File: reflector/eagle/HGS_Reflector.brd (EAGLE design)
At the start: 100 x 100 mm, 27 parts, among them J1 U.FL, U3 LP2985XX-N

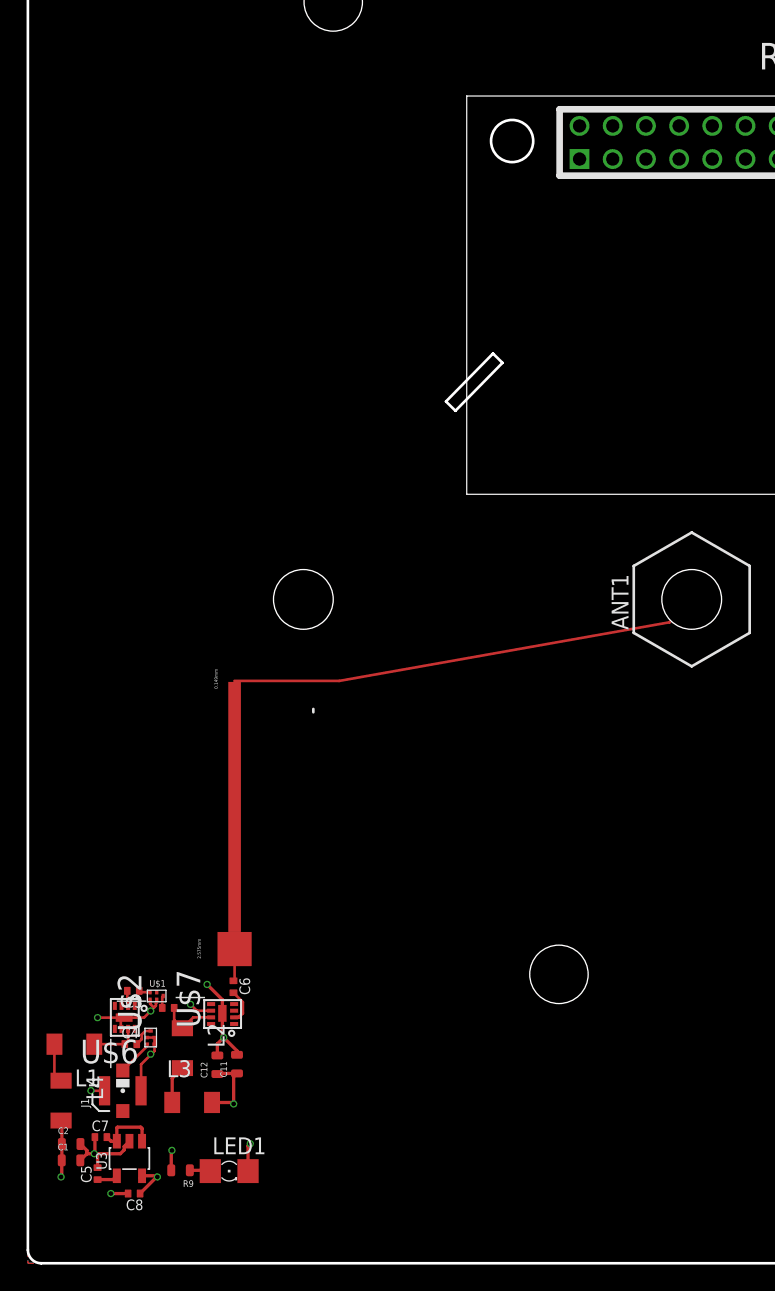
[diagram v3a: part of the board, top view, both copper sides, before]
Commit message: On the HGS board, I positioned the 3.3V regulator so that it is now close to the pin header on the Rasp Pi Zero W, and made a few changes to positions of the other parts to accomodate that.
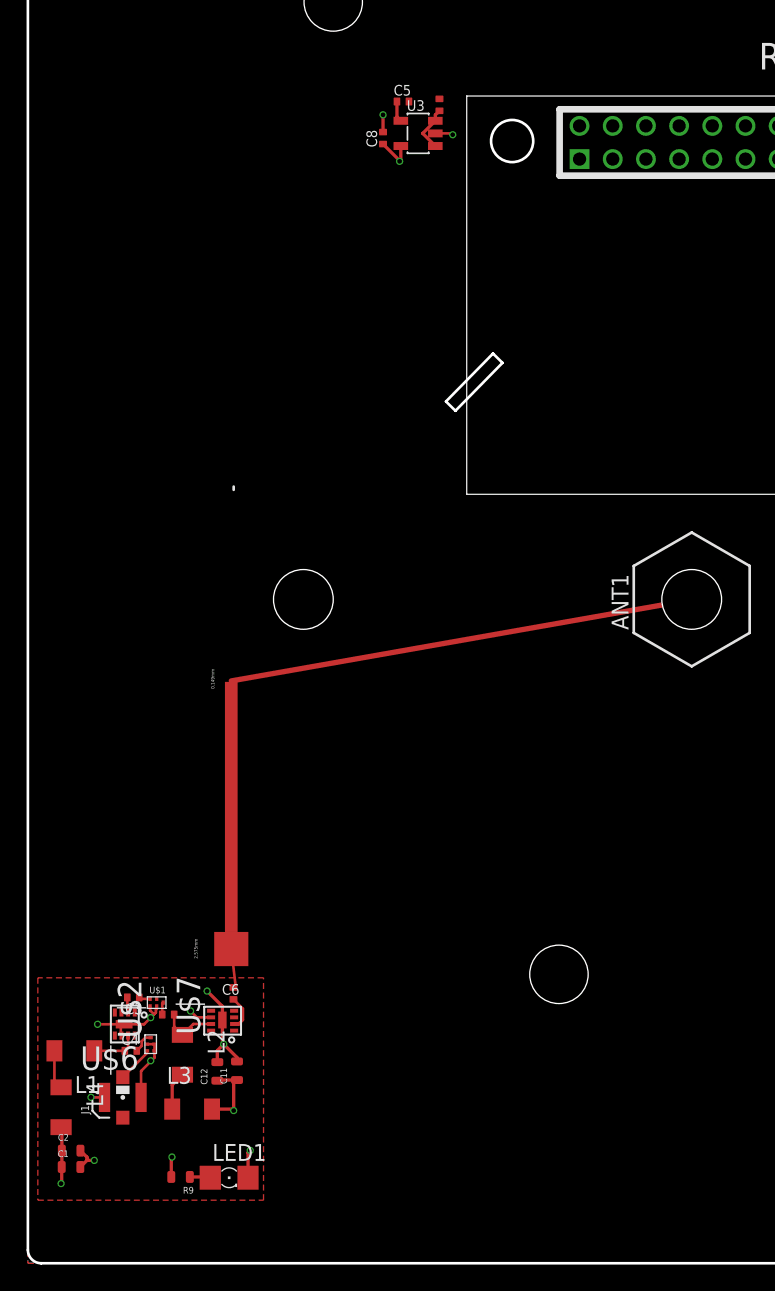
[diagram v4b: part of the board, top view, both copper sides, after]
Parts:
- moved C5 84.0 mm to (28.2, 87.5), turned to 0 degrees
- moved C7 81.8 mm to (31.0, 87.2), turned to 270 degrees
- moved C8 81.7 mm to (26.8, 84.8), turned to 90 degrees
- moved U3 80.2 mm to (29.4, 85.1), turned to 180 degrees
- moved C1 0.50 mm to (3.25, 7.25)
- moved C11 0.50 mm to (15.8, 14.5)
- moved C12 0.50 mm to (14.3, 14.4)
- moved C14 0.50 mm to (10.6, 18.7)
- moved C2 0.50 mm to (3.26, 8.48)
- moved C3 0.50 mm to (7.94, 20.0)
- moved C4 0.50 mm to (7.75, 16.0)
- moved C6 0.50 mm to (15.5, 20.3)
- moved J1 0.50 mm to (7.15, 12.5)
- moved L1 0.50 mm to (3.50, 16.0)
- moved L2 0.50 mm to (11.6, 15.7)
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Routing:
- net GND: track 33.5 -> 29.4 mm, vias 10 -> 11
- net 5V: track 4.81 -> 3.57 mm
- net N$9: track 2.42 -> 3.12 mm

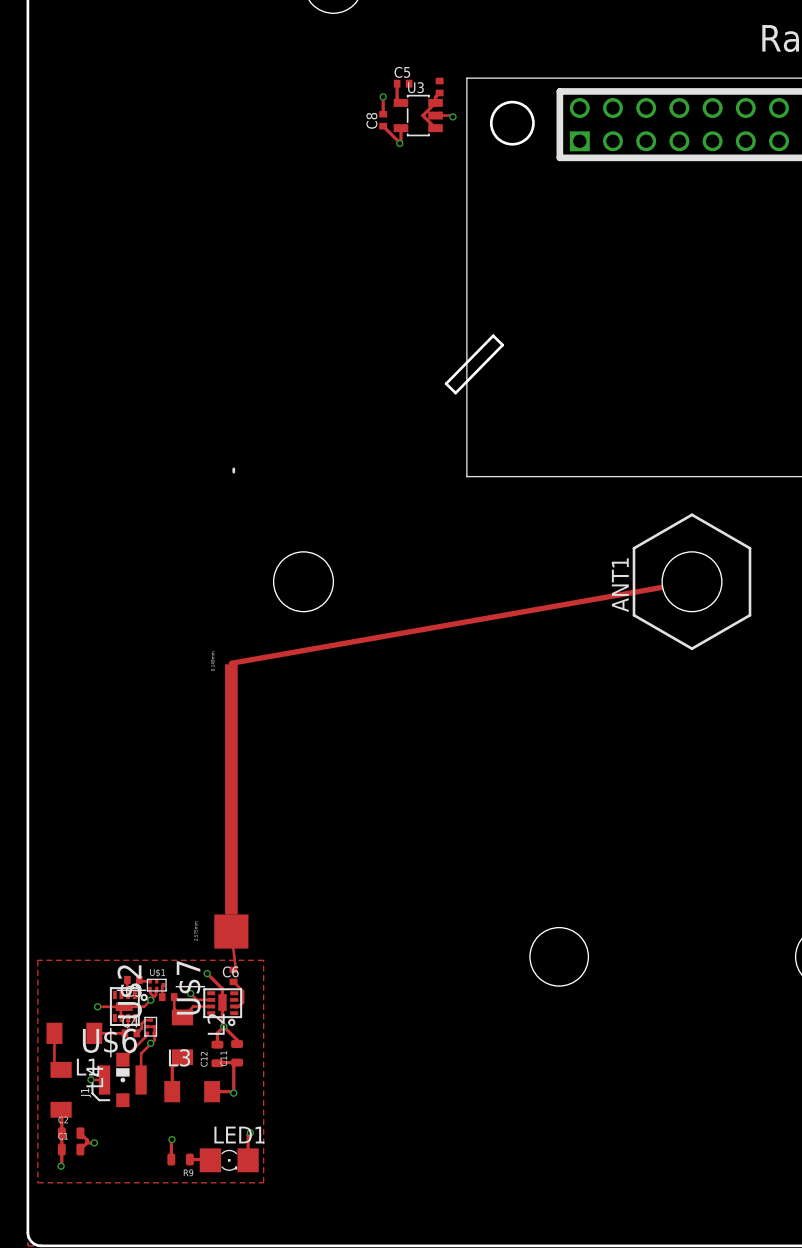
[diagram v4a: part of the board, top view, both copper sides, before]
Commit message: I made sure that all the signals were completely routed, and fixed the clearance issue with the wire going to the center by replacing the center drill hole with a large via that goes directly to the antenna footprint on the top of the board (layer 16).
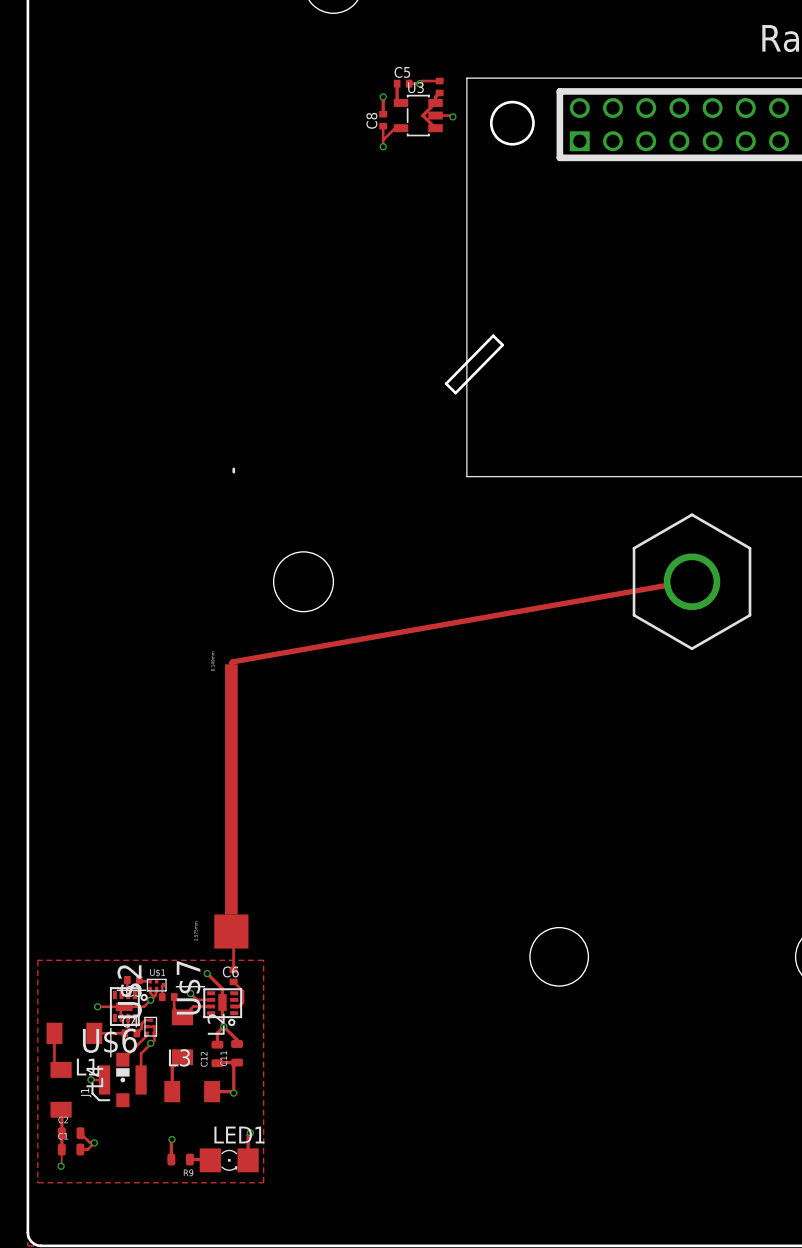
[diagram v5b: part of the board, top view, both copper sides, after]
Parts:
- flipped ANT1 to the bottom
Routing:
- net GND: track 29.4 -> 32.1 mm, vias 11 -> 12
- net N$2: vias 0 -> 1
- added copper zone on layer 15, net 3.3V
- removed copper zone on layer 15, net GND

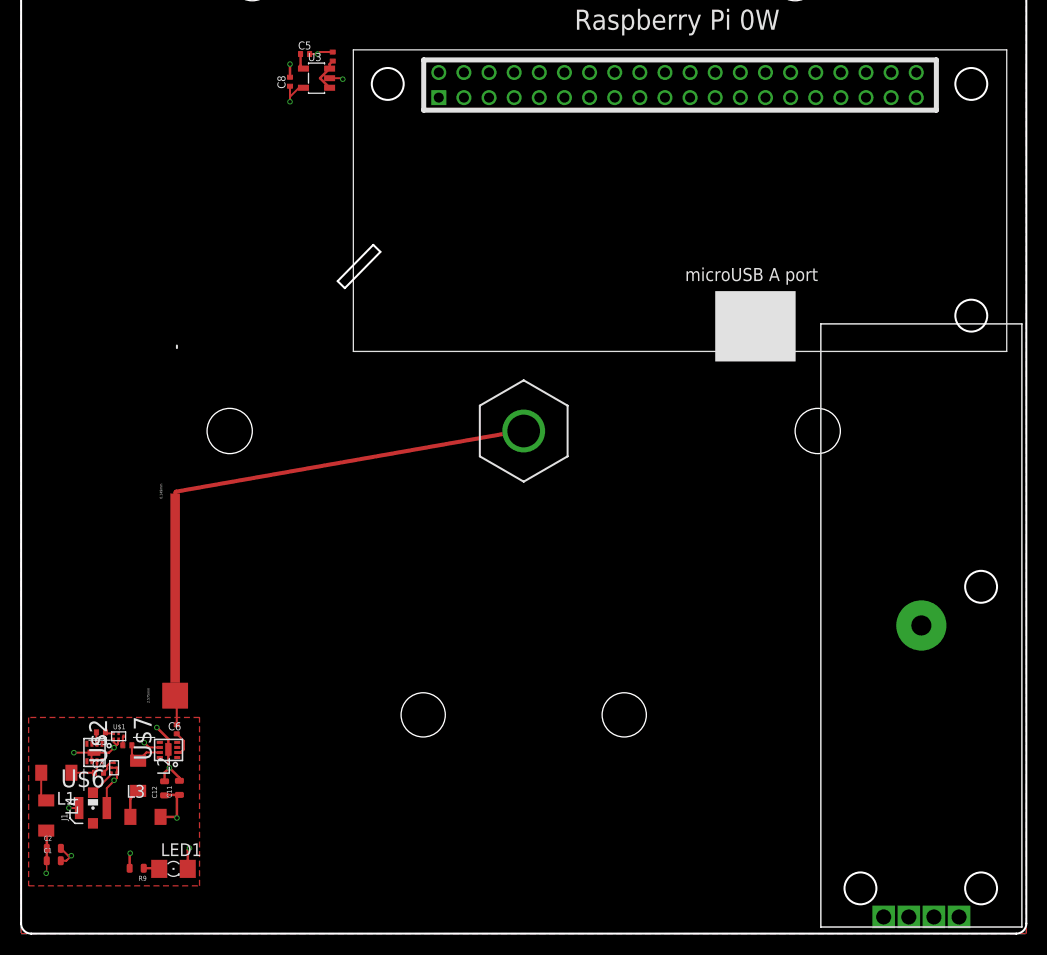
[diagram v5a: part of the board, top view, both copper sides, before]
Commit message: I finalized the schematic and routing of the board for HGS. Note that I adjusted the dxf layer by adding a fourth drill hole underneath the atheros card. It is ready for a design review.
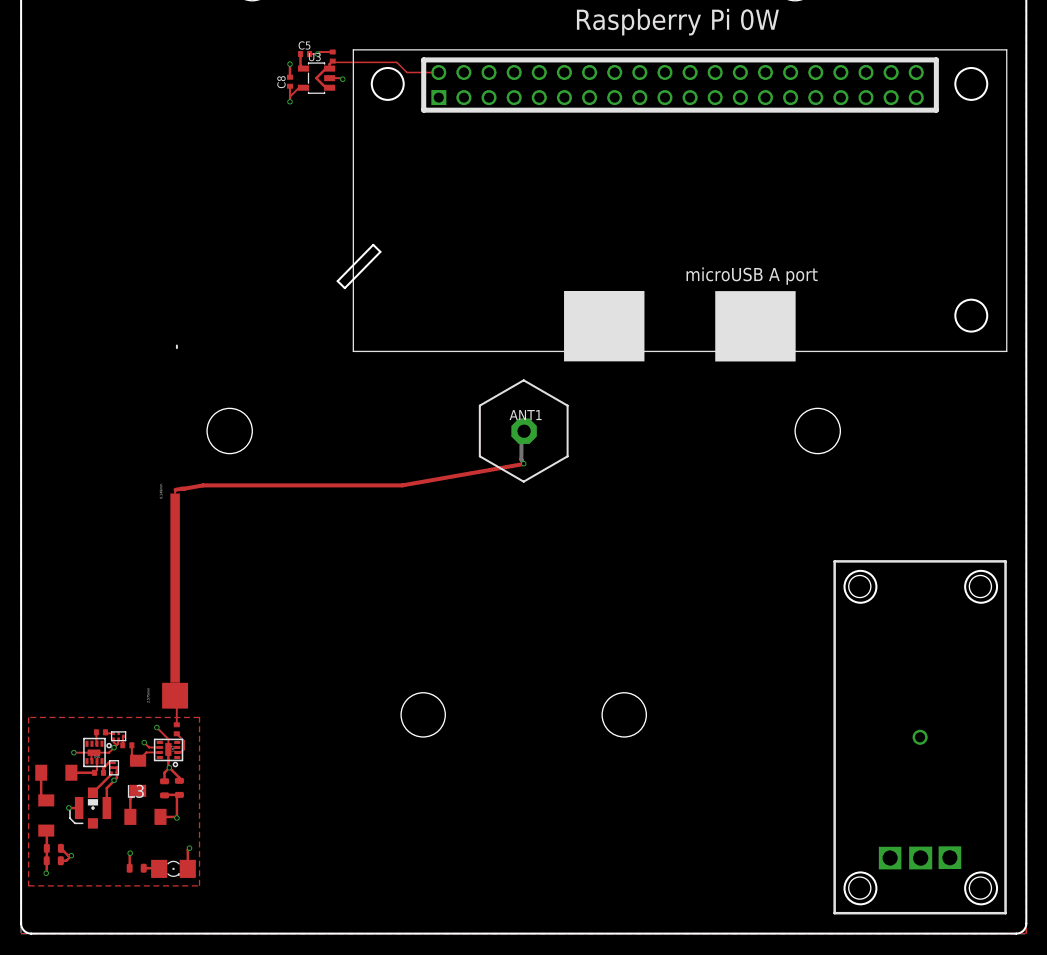
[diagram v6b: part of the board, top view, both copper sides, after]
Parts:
- U$4: value AR9721 -> AR9721WF; device AR9721:AR9721 -> AR9721:WF-NP9202
- moved U$4 11.1 mm to (89.4, 19.5)
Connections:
- removed net 1: U$4.GND
- removed net 5V: C7.2, U3.1, U3.3
- removed net N$18: U$4.D+
- removed net N$19: U$4.D-
- removed net VCC: U$4.VCC
- new net N$12: C7.2, U$5.5V, U3.1, U3.3
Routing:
- net N$12: track 0.00 -> 15.3 mm
- net 5V: track 3.57 -> 0.00 mm
- net N$2: track 35.3 -> 38.6 mm
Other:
- outline, holes or cut-outs redrawn
- board text added: "LNA-TP3M9037"

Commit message: Fixed keepout zones, removed antenna through hole, put 1/4 wave transformer in the right place, but, this is going to be totally hoky. Is there a better way?
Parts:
- moved U$3 29.0 mm to (20.0, 63.0), turned to 0 degrees
- moved ANT1 12.5 mm to (37.5, 50.5), flipped to the top
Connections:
- net N$2: no longer ANT1.1
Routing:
- net N$2: track 38.6 -> 3.01 mm, vias 1 -> 0
- net GND: vias 12 -> 62
- added copper zone on layer 15, net GND
- added copper zone on layer 1, net KEEPOUT
- added copper zone on layer 2, net KEEPOUT
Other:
- outline, holes or cut-outs redrawn
